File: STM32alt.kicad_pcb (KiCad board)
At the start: 2 copper layers, 25.7 x 78.7 mm, 29 parts, among them J3 USB_B, J4 Conn_01x04, J5 Conn_01x20, J7 Conn_01x02, J9 Conn_01x20, U1 LM1117-3.3, U2 STM32f405RGT6, Y1 8 MHz, Y2 Crystal

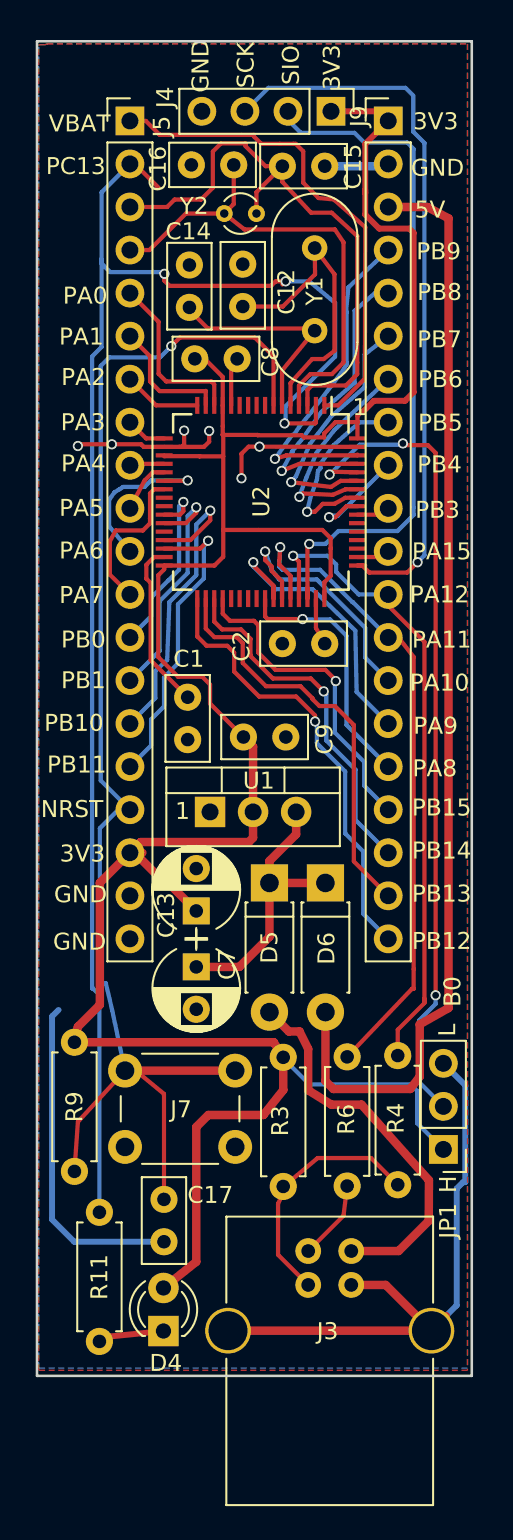
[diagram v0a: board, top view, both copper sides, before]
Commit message: Added pull down on BOOT1
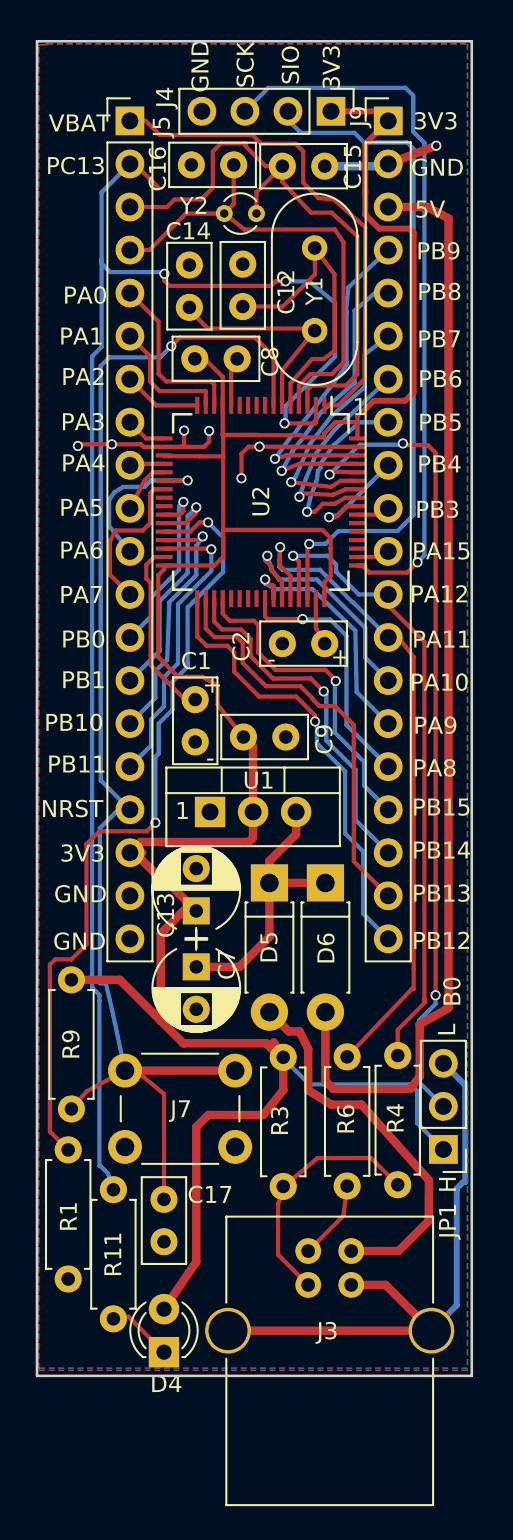
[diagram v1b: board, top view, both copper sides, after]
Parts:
- added R1: 100k, Resistors_THT:R_Axial_DIN0207_L6.3mm_D2.5mm_P7.62mm_Horizontal, F.Cu at (57.5, 94.9)
- moved R9 3.69 mm to (57.7, 84.8)
- moved R11 1.57 mm to (60.1, 97.2)
- moved D4 1.25 mm to (63.1, 106.8)
- moved C1 0.47 mm to (65.0, 70.8)
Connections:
- U2 pad 28: (no net) -> Net-(R1-Pad1)
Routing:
- net Net-(R1-Pad1): track 0.00 -> 47.3 mm, vias 0 -> 2
- net GNDB: track 81.4 -> 64.7 mm, vias 6 -> 7
- net NRST: track 81.1 -> 78.1 mm
- net PB10: track 18.3 -> 15.4 mm
- net PA9: track 17.5 -> 15.2 mm
- net PC13: track 92.2 -> 91.1 mm
- net Net-(C1-Pad2): track 10.1 -> 10.7 mm
- net PA10: track 15.0 -> 14.5 mm
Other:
- board text added: "+"
- board text added: "-"
